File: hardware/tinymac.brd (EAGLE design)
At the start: 43 x 41.4 mm, 29 parts, among them IC1 LPC1114FN28, J1 ZX62-B-5PA, SW1 TACT_SW, SW2 TACT_SW, SW3 TACT_SW, SW4 TACT_SW, SW5 TACT_SW, T1 TA48M033F

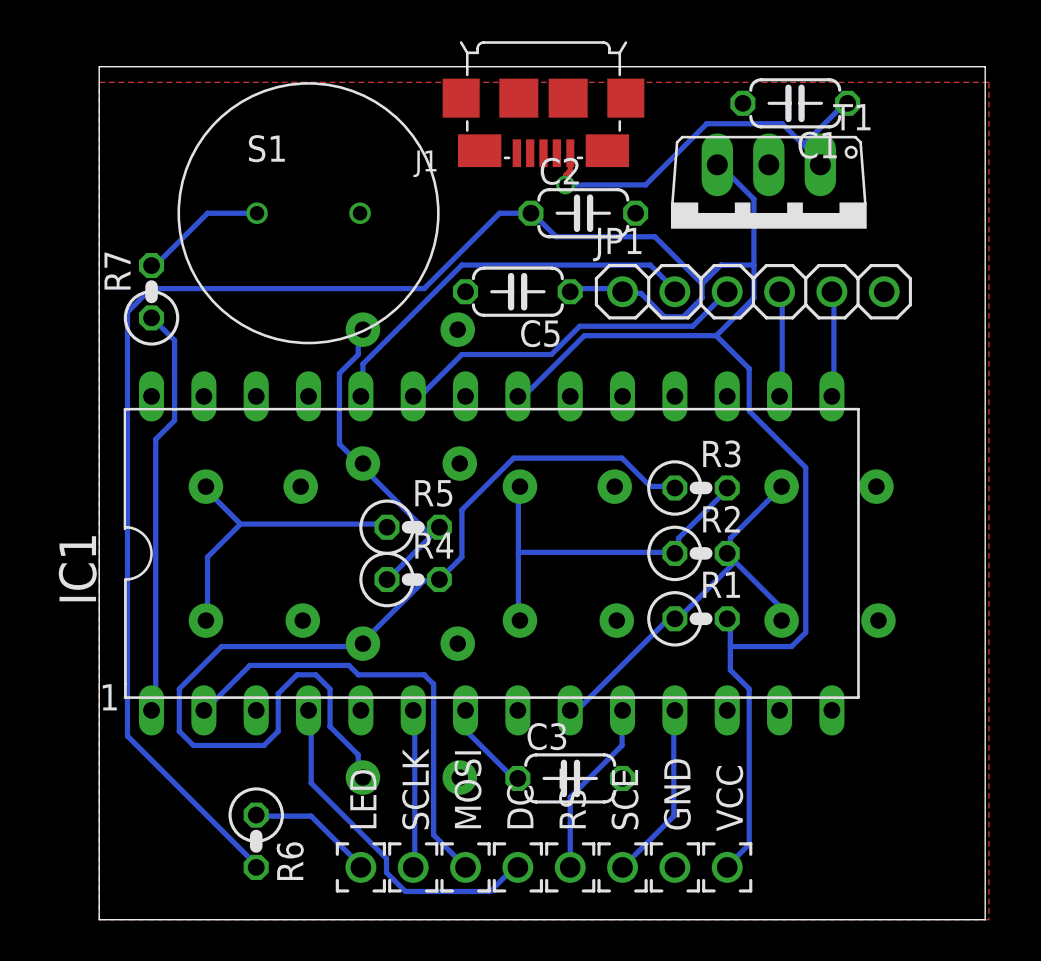
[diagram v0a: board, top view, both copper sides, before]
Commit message: add screw hole
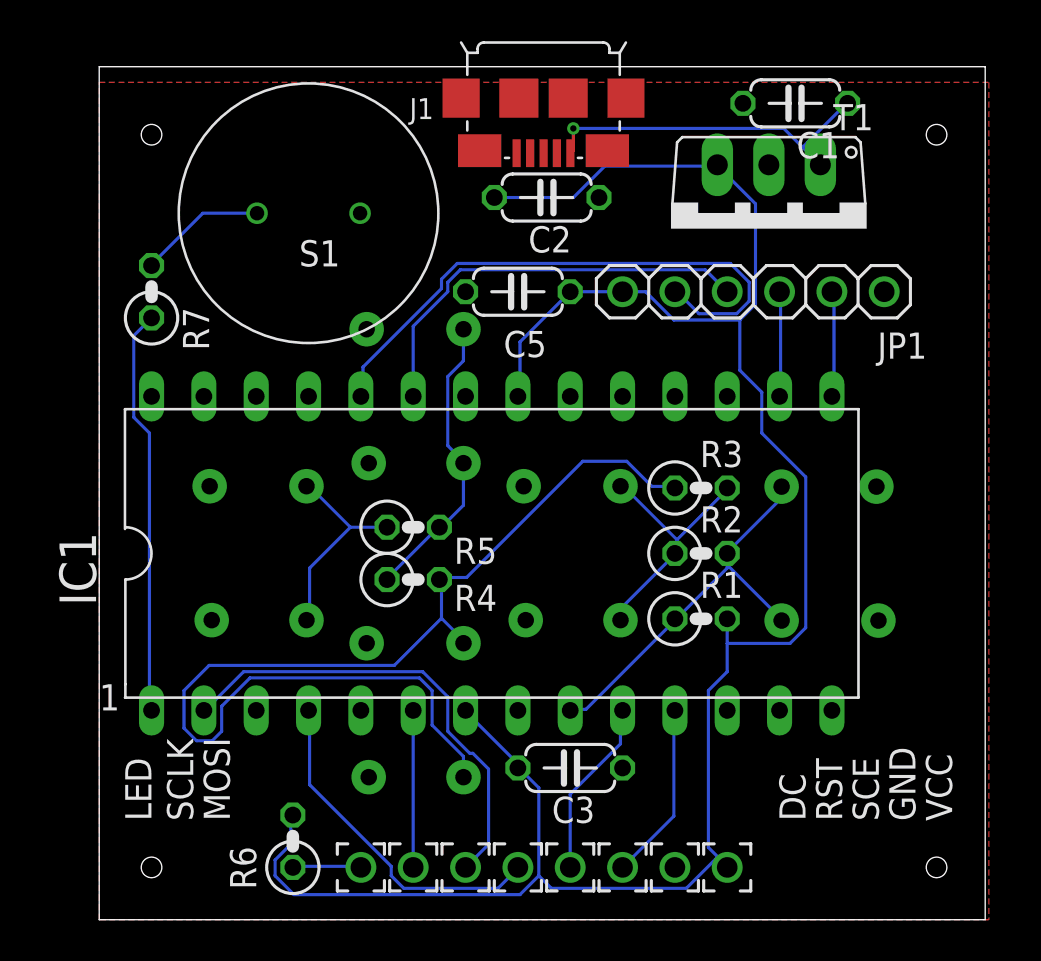
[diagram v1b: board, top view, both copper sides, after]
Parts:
- moved C2 1.93 mm to (21.7, 35.1)
- moved R6 1.78 mm to (9.40, 3.81), turned to 90 degrees
- moved C3 0.51 mm to (22.9, 7.37)
- turned SW2 to 0 degrees
- turned SW3 to 0 degrees
- turned SW4 to 0 degrees
- turned SW5 to 0 degrees
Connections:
- removed net +3.3V_TGT: C3.1, IC1.7
- net +3.3V: now also C3.1, IC1.7
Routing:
- net +3.3V: track 125.8 -> 105.0 mm
- net N$17: track 19.3 -> 28.2 mm
- net N$2: track 18.6 -> 12.5 mm
- net N$8: track 15.1 -> 10.1 mm
- net N$6: track 48.3 -> 53.2 mm
- net +3.3V_TGT: track 4.46 -> 0.00 mm
- net N$18: track 17.4 -> 20.5 mm
- net N$19: track 6.15 -> 3.34 mm
- net N$7: track 16.8 -> 14.5 mm
- net VBUS: track 19.2 -> 17.1 mm
- net N$15: track 20.4 -> 19.5 mm
- net N$4: track 21.9 -> 22.8 mm

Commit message: fix board register position overlap
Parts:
- moved R4 21.4 mm to (33.0, 28.4)
- moved R5 15.4 mm to (27.4, 28.4)
- moved R2 13.7 mm to (40.6, 25.4), turned to 90 degrees
- moved R3 12.3 mm to (39.1, 28.3)
- moved R1 12.1 mm to (40.5, 10.4), turned to 270 degrees
- moved JP1 1.44 mm to (32.8, 31.5)
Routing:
- net +3.3V: track 105.0 -> 0.00 mm
- net N$6: track 53.2 -> 0.00 mm
- net N$17: track 28.2 -> 0.00 mm
- net N$4: track 22.8 -> 0.00 mm
- net N$18: track 20.5 -> 0.00 mm
- net N$13: track 19.8 -> 0.00 mm
- net N$15: track 19.5 -> 0.00 mm
- net VBUS: track 17.1 -> 0.00 mm, vias 1 -> 0
- net N$9: track 16.5 -> 0.00 mm
- net N$7: track 14.5 -> 0.00 mm
- net N$2: track 12.5 -> 0.00 mm
- net N$8: track 10.1 -> 0.00 mm
- net N$10: track 8.67 -> 0.00 mm
- net N$12: track 8.66 -> 0.00 mm
- net N$5: track 7.62 -> 0.00 mm
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
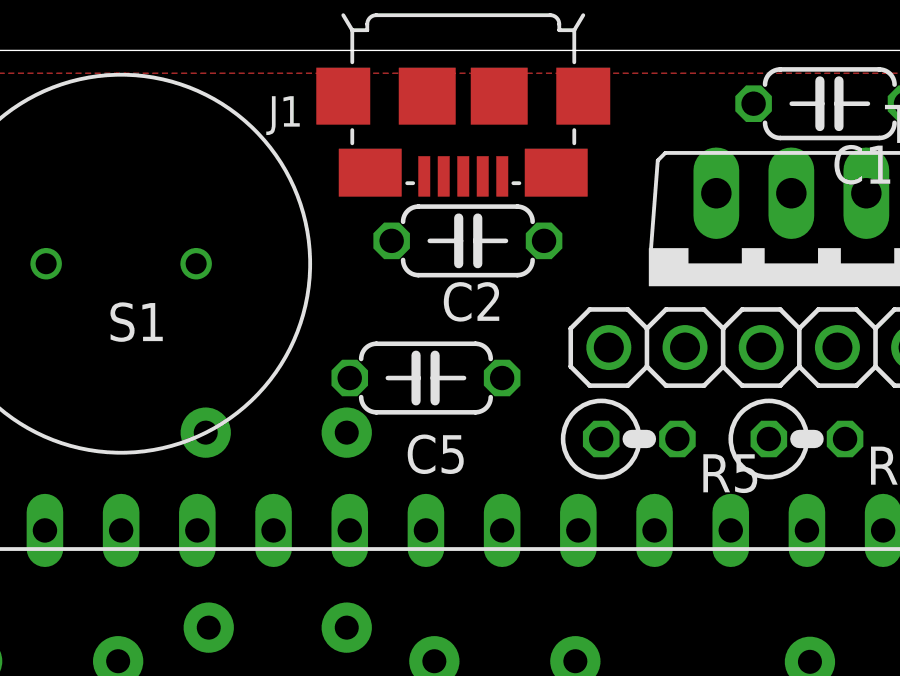
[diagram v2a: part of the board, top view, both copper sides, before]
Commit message: replace capacitor C2
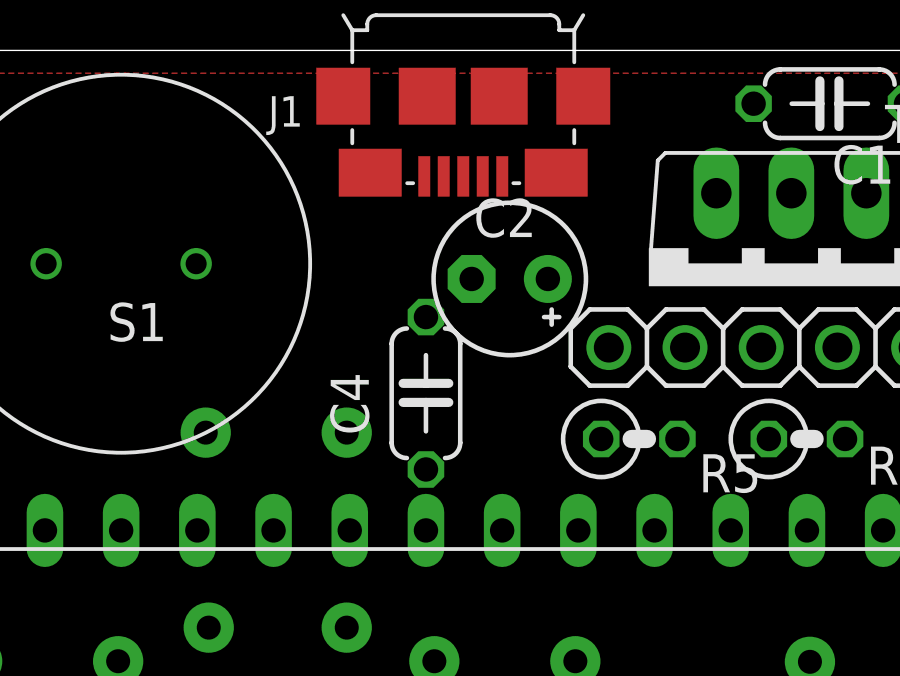
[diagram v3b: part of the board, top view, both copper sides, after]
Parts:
- removed C5: 0.1uF, maclock:C050-024X044
- added C4: 0.1uF, maclock:C050-024X044
- C2: device maclock:C050-024X044 -> tinymac:E2,5-5
- moved C2 1.89 mm to (23.1, 33.8), turned to 180 degrees
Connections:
- net +3.3V: now also C2.+, C4.1; no longer C2.1, C5.1
- net GND: now also C2.-, C4.2; no longer C2.2, C5.2
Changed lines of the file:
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@@
 <setting verticaltext="up"/>
 </settings>
-<grid distance="0.1" unitdist="inch" unit="mm" style="lines" multiple="1" display="yes" altdistance="0.01" altunitdist="inch" altunit="inch"/>
+<grid distance="0.1" unitdist="inch" unit="inch" style="lines" multiple="1" display="yes" altdistance="0.01" altunitdist="inch" altunit="inch"/>
 <layers>
 <layer number="1" name="Top" color="4" fill="1" visible="yes" active="yes"/>
@@
 <layer number="220" name="220bmp" color="21" fill="1" visible="no" active="no"/>
 <layer number="221" name="221bmp" color="22" fill="1" visible="no" active="no"/>
+<layer number="222" name="imagesize" color="7" fill="1" visible="no" active="yes"/>
 <layer number="223" name="223bmp" color="24" fill="1" visible="no" active="no"/>
 <layer number="224" name="224bmp" color="25" fill="1" visible="no" active="no"/>
@@
 <element name="T1" library="tinymac" package="TA48M033F" value="TA48M033F" x="32.5" y="33.54" rot="R180"/>
 <element name="C1" library="tinymac" package="C050-024X044" value="0.1uF" x="33.782" y="39.624" rot="R180"/>
-<element name="C2" library="maclock" package="C050-024X044" value="47uF" x="21.717" y="35.052" smashed="yes">
-<attribute name="NAME" x="20.828" y="32.385" size="1.27" layer="25" ratio="10"/>
+<element name="C2" library="tinymac" package="E2,5-5" value="47uF" x="23.114" y="33.782" smashed="yes" rot="R180">
+<attribute name="NAME" x="24.003" y="36.449" size="1.27" layer="25" ratio="10" rot="R180"/>
 </element>
 <element name="SW1" library="tinymac" package="TACT_SW" value="TACT_SW" x="35.56" y="17.78" smashed="yes" rot="MR180">
@@
 <attribute name="NAME" x="29.4132" y="26.67" size="1.27" layer="25" ratio="10"/>
 </element>
-<element name="C5" library="maclock" package="C050-024X044" value="0.1uF" x="20.32" y="30.48" smashed="yes" rot="R180">
-<attribute name="NAME" x="21.717" y="28.575" size="1.27" layer="25" ratio="10" rot="R180"/>
+<element name="C4" library="maclock" package="C050-024X044" value="0.1uF" x="20.32" y="29.972" smashed="yes" rot="R90">
+<attribute name="NAME" x="18.415" y="28.575" size="1.27" layer="25" ratio="10" rot="R90"/>
 </element>
 <element name="LED" library="tinymac2" package="HOLE_PAD" value="" x="12.7" y="2.54" smashed="yes" rot="R90">
@@
 <contactref element="C1" pad="2"/>
 <contactref element="T1" pad="2"/>
-<contactref element="C2" pad="2"/>
+<contactref element="C2" pad="-"/>
 <contactref element="GND" pad="1"/>
 <contactref element="SW3" pad="1-B"/>
@@
 <contactref element="SW4" pad="2-B"/>
 <contactref element="JP1" pad="6"/>
-<contactref element="C5" pad="2"/>
+<contactref element="C4" pad="2"/>
 <contactref element="J1" pad="SH3"/>
 <contactref element="J1" pad="SH4"/>
@@
 <signal name="+3.3V">
 <contactref element="T1" pad="3"/>
-<contactref element="C2" pad="1"/>
+<contactref element="C2" pad="+"/>
 <contactref element="JP1" pad="1"/>
-<contactref element="C5" pad="1"/>
+<contactref element="C4" pad="1"/>
 <contactref element="IC1" pad="21"/>
 <contactref element="VCC" pad="1"/>
@@
 <contactref element="C3" pad="1"/>
 <wire x1="26.416" y1="31.496" x2="30" y2="36.64" width="0" layer="19" extent="1-1"/>
-<wire x1="22.86" y1="30.48" x2="26.416" y2="31.496" width="0" layer="19" extent="1-1"/>
-<wire x1="20.32" y1="25.4" x2="22.86" y2="30.48" width="0" layer="19" extent="1-1"/>
-<wire x1="19.177" y1="35.052" x2="22.86" y2="30.48" width="0" layer="19" extent="1-1"/>
+<wire x1="24.384" y1="33.782" x2="26.416" y2="31.496" width="0" layer="19" extent="1-1"/>
+<wire x1="20.32" y1="27.432" x2="26.416" y2="31.496" width="0" layer="19" extent="1-1"/>
+<wire x1="20.32" y1="25.4" x2="20.32" y2="27.432" width="0" layer="19" extent="1-1"/>
 <wire x1="17.78" y1="10.16" x2="20.32" y2="25.4" width="0" layer="19" extent="1-1"/>
 <wire x1="20.32" y1="7.366" x2="17.78" y2="10.16" width="0" layer="19" extent="1-1"/>

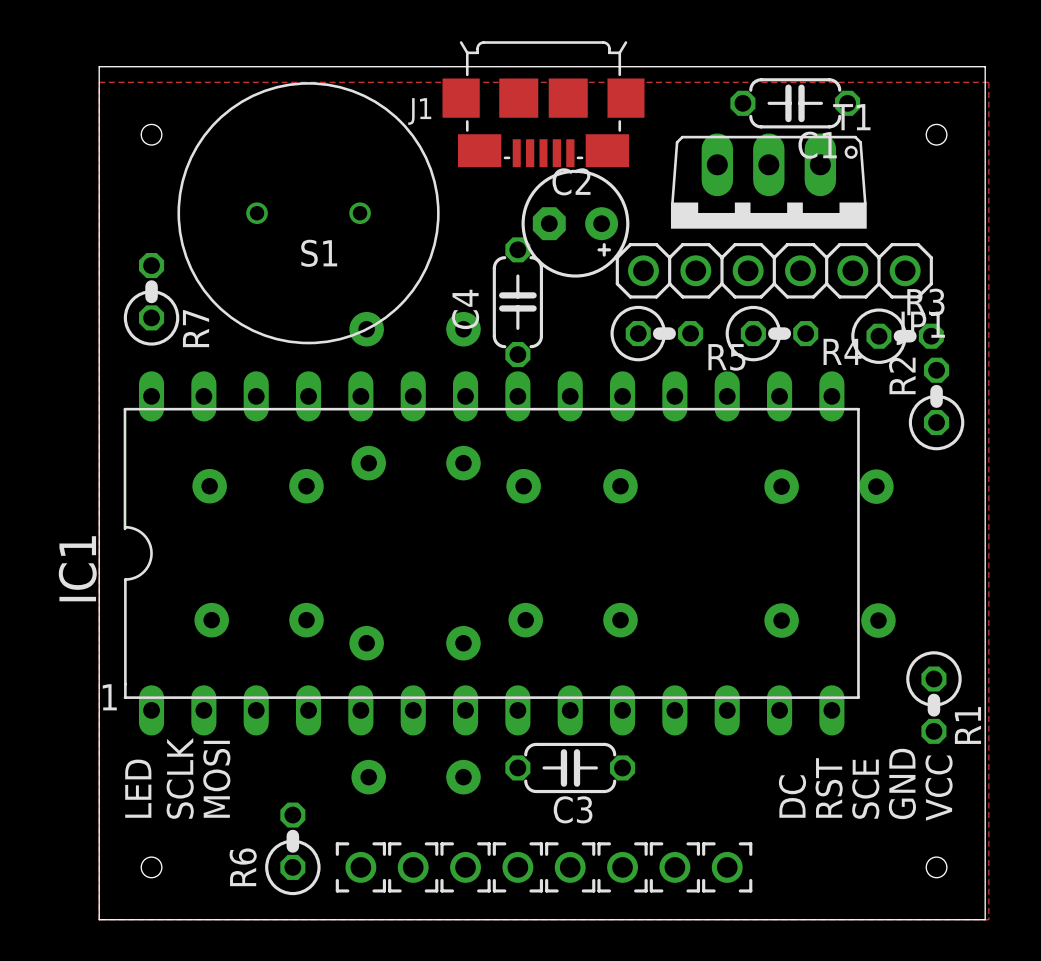
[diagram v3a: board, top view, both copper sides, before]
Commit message: move full GND to bottom layer
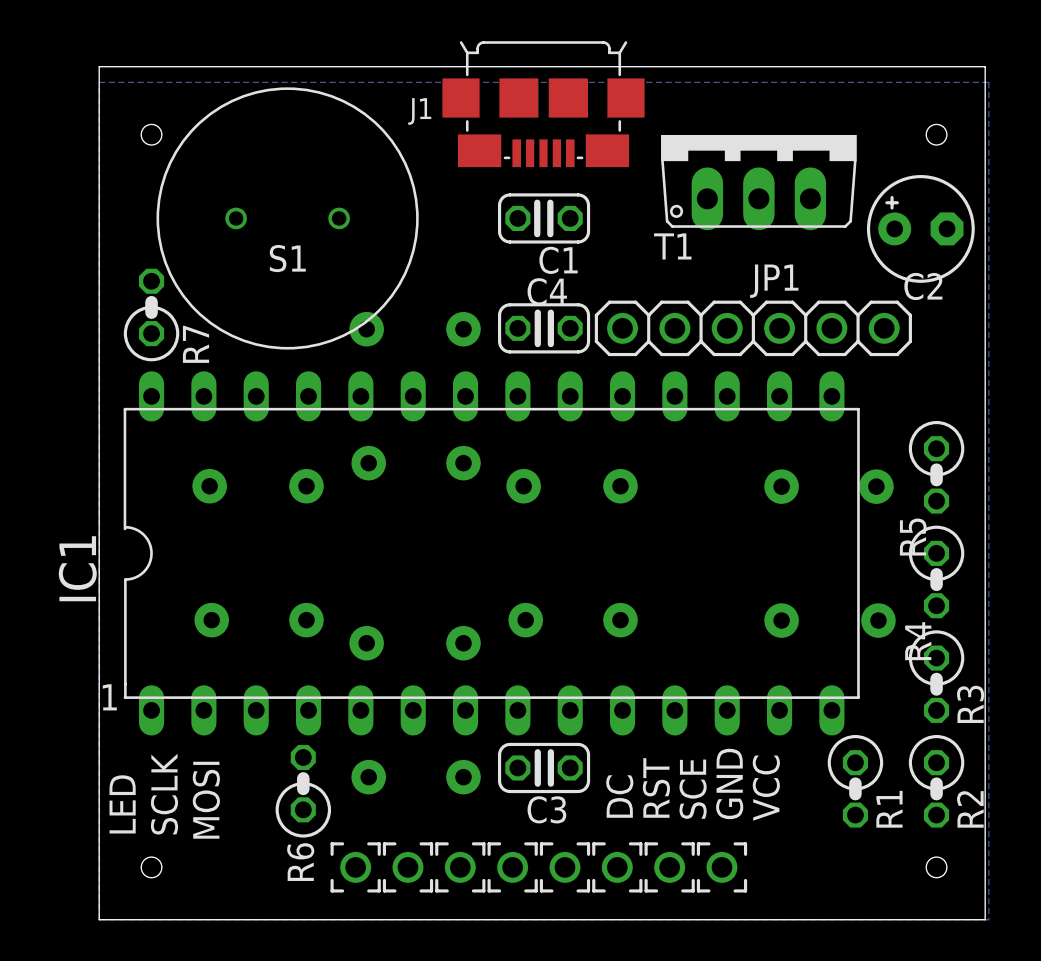
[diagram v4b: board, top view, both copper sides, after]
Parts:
- C1: device tinymac:C050-024X044 -> tinymac:C025-024X044
- C3, C4: device maclock:C050-024X044 -> tinymac:C025-024X044
- moved R2 19.0 mm to (40.6, 6.35), turned to 270 degrees
- moved R3 17.0 mm to (40.6, 11.4), turned to 270 degrees
- moved C2 16.8 mm to (39.9, 33.5), turned to 0 degrees
- moved R5 14.9 mm to (40.6, 21.6), turned to 270 degrees
- moved R4 14.2 mm to (40.6, 16.5), turned to 270 degrees
- moved C1 13.4 mm to (21.6, 34.0)
- moved R1 5.57 mm to (36.7, 6.35)
- moved T1 4.57 mm to (32.0, 38.1), turned to 0 degrees
- moved JP1 2.97 mm to (31.8, 28.7)
- moved R6 2.84 mm to (9.91, 6.60)
- moved C4 1.80 mm to (21.6, 28.7), turned to 0 degrees
- moved C3 1.27 mm to (21.6, 7.37)
- moved S1 1.05 mm to (9.14, 34.0)
- moved R7 0.76 mm to (2.54, 29.7)
- moved DC 0.25 mm to (20.1, 2.54)
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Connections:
- net N$15: now also R2.1; no longer R2.2
- net N$2: now also R2.2; no longer R2.1
- net N$7: now also R5.1; no longer R5.2
- net N$8: now also R5.2; no longer R5.1
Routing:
- added copper zone on layer 16, net GND
- removed copper zone on layer 1, net GND

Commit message: set net classes properties
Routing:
- net +3.3V: track 0.00 -> 92.8 mm
- net N$8: track 0.00 -> 49.5 mm
- net N$15: track 0.00 -> 47.3 mm
- net N$6: track 0.00 -> 41.5 mm
- net N$7: track 0.00 -> 39.2 mm
- net N$2: track 0.00 -> 29.5 mm
- net N$4: track 0.00 -> 21.1 mm
- net GND: track 0.00 -> 19.3 mm
- net N$13: track 0.00 -> 19.0 mm
- net N$18: track 0.00 -> 16.6 mm
- net N$17: track 0.00 -> 16.6 mm
- net N$9: track 0.00 -> 16.5 mm
- net VBUS: track 0.00 -> 9.83 mm
- net N$12: track 0.00 -> 8.81 mm
- net N$10: track 0.00 -> 8.81 mm
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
